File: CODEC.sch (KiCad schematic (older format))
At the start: 1 part

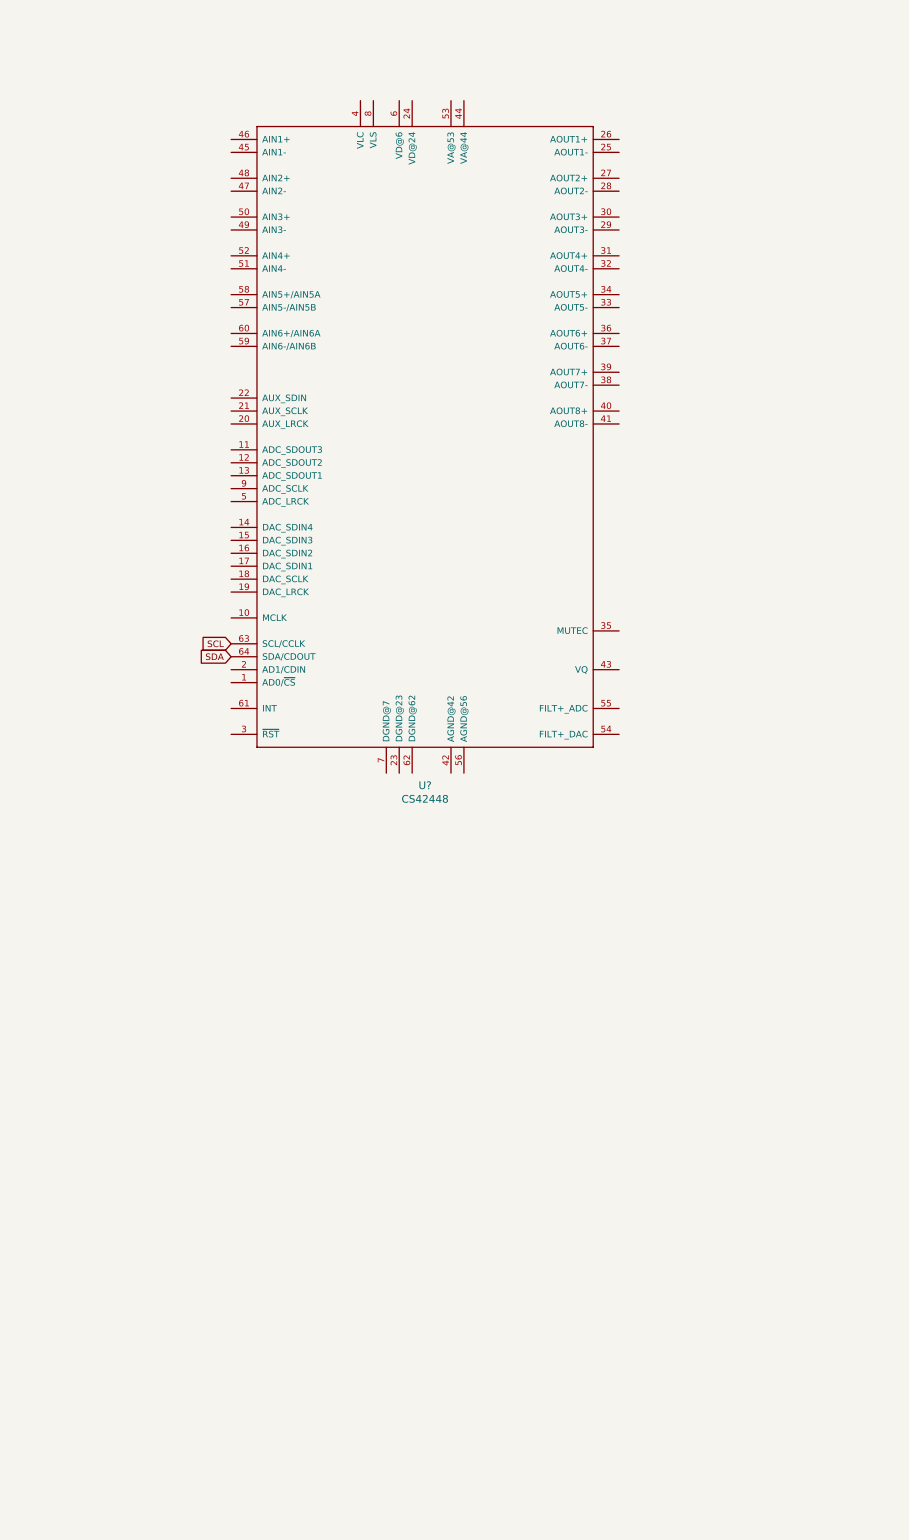
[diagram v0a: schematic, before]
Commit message: - Cleaned up schematic layout by creating dedicated sheet for codec as   well as analog input filters in addition to the main Teensy sheet - Added schematics for all AIN filters based on codec datasheet - Added dedicated 3v3 supply and gave all supplies power flags. Created   dedicated digital/analog GND as well as recommended 3v3A for codec power
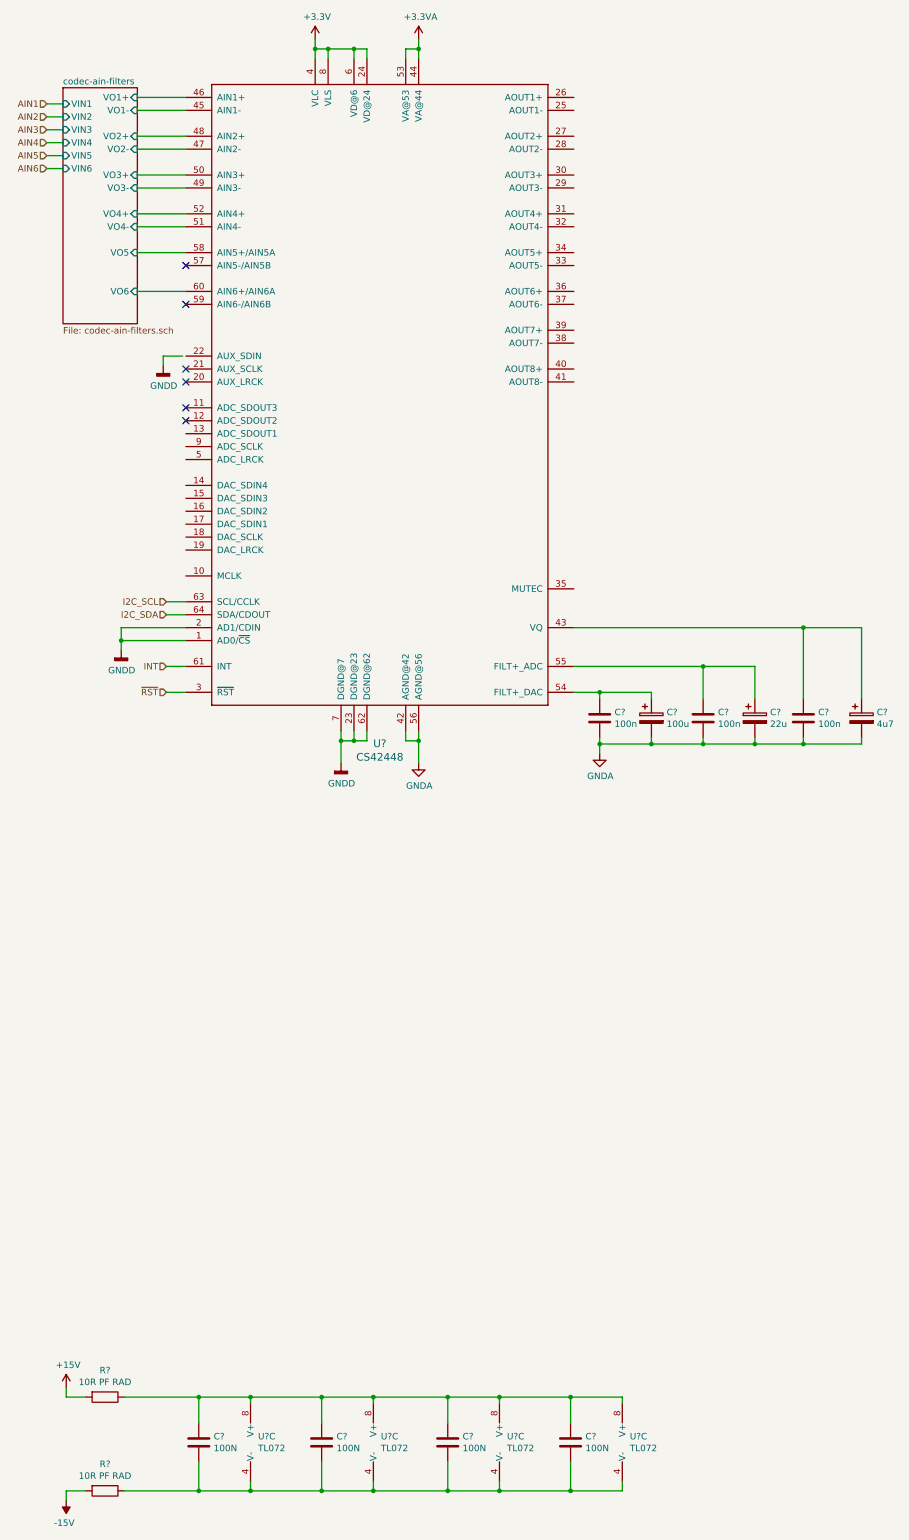
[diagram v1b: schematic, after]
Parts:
- added C? (x4): 100N, symbol Device:C
- added C? (x3): 100n, symbol Device:C
- added C?: 100u, symbol Device:CP
- added C?: 22u, symbol Device:CP
- added C?: 4u7, symbol Device:CP
- added R? (x2): 10R PF RAD, symbol Device:R
- added U? (x4): TL072, symbol Amplifier_Operational:TL072
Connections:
- net GNDD: now reaches U?.1 (AD0/~CS~)
- net GNDD: now also U?.2 (AD1/CDIN), U?.23 (DGND@23), U?.62 (DGND@62), U?.7 (DGND@7)
- net +3V3: now reaches U?.24 (VD@24)
- net +3V3: now also U?.4 (VLC), U?.6 (VD@6), U?.8 (VLS)
- net ~RST: now reaches U?.3 (~RST~)
- net GNDA: now reaches U?.42 (AGND@42)
- net GNDA: now also U?.56 (AGND@56), C?.2, C?.2, C?.2, C?.2, C?.2, C?.2
- net at U?.43 (VQ): now also C?.1, C?.1
- net +3.3VA: now reaches U?.44 (VA@44)
- net +3.3VA: now also U?.53 (VA@53)
- net codec-ain-filters/VO1-: now reaches U?.45 (AIN1-)
- net codec-ain-filters/VO1+: now reaches U?.46 (AIN1+)
- net codec-ain-filters/VO2-: now reaches U?.47 (AIN2-)
- net codec-ain-filters/VO2+: now reaches U?.48 (AIN2+)
- net codec-ain-filters/VO3-: now reaches U?.49 (AIN3-)
- net codec-ain-filters/VO3+: now reaches U?.50 (AIN3+)
- net codec-ain-filters/VO4-: now reaches U?.51 (AIN4-)
- net codec-ain-filters/VO4+: now reaches U?.52 (AIN4+)
- net at U?.54 (FILT+_DAC): now also C?.1, C?.1
- net at U?.55 (FILT+_ADC): now also C?.1, C?.1
- net codec-ain-filters/VO5: now reaches U?.58 (AIN5+/AIN5A)
- net codec-ain-filters/VO6: now reaches U?.60 (AIN6+/AIN6A)
- net INT: now reaches U?.61 (INT)
- net SCL renamed I2C_SCL
- net SDA renamed I2C_SDA
- new net: C?.1, C?.1, C?.1, C?.1, R?.1, U?.8 (V+), U?.8 (V+), U?.8 (V+), U?.8 (V+)
- new net: C?.2, C?.2, C?.2, C?.2, R?.1, U?.4 (V-), U?.4 (V-), U?.4 (V-), U?.4 (V-)
- new net +15V: R?.2
- new net -15V: R?.2
- no-connect marks 0 -> 6
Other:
- moved on the sheet: U?
